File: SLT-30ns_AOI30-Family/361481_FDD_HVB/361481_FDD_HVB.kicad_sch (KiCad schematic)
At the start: 9 parts, among them U1 12-Pin_SLx_Can

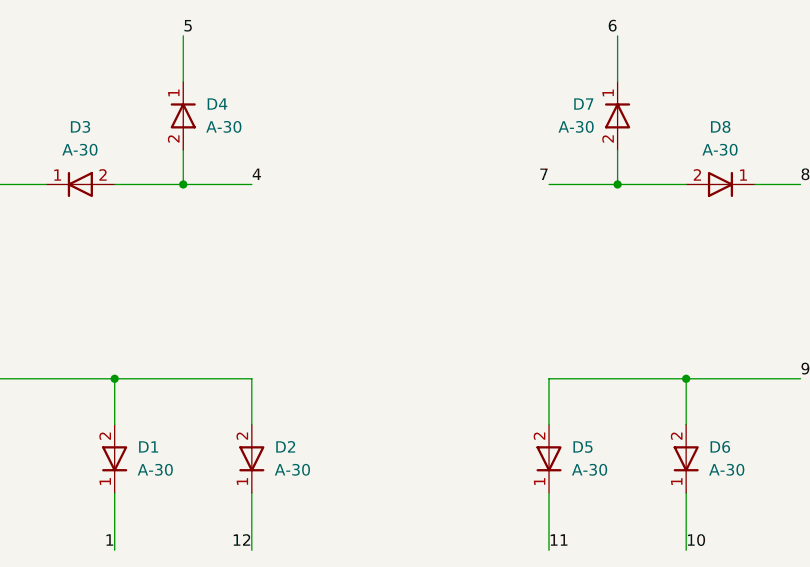
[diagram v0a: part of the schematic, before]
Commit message: Update schematic pdfs
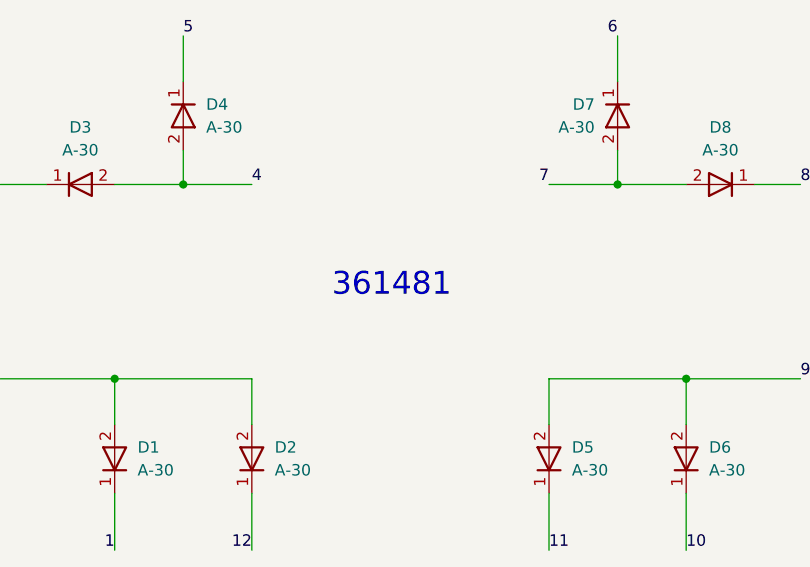
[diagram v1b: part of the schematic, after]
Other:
- note added: "361481"
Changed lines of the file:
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@@
     (effects (font (size 1.27 1.27)) (justify left bottom))
+  )
+  (text "361481" (at 113.03 92.71 0)
+    (effects (font (size 2.54 2.54)) (justify left bottom))
   )
   (label "9" (at 248.92 137.16 0)
